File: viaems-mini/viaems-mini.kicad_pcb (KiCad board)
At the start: 2 copper layers, 214 parts, among them J1 Power Drivers, J10 TEST, J11 Sensors, J12 Debug, J13 USB_B_Micro, J14 Micro_SD_Card, J2 Primary, J3 Ignition Trace, J4 Injector Trace, J5 GPIO58, J6 SPI1, J7 PORTC, J8 PWM56, J9 CAN2, Q1 VNL5090S5-E, Q10 VNL5090S5-E, Q11 VNL5090S5-E, Q12 VNL5090S5-E, Q13 VNL5090S5-E, Q14 VNL5090S5-E, Q15 VNL5090S5-E, Q16 VNL5090S5-E, Q2 VNL5090S5-E, Q3 VNL5090S5-E, Q4 VNL5090S5-E, Q5 VNL5090S5-E, Q6 VNL5090S5-E, Q7 VNL5090S5-E, Q8 VNL5090S5-E, Q9 VNL5090S5-E, U1 TJA1051T-3, U10 MAX9926UAEE+, U11 LM2937-N, U2 LM2937-N, U3 NCV5501, U4 STM32F427VGTx, U5 MIC4469, U6 MIC4469, U7 MPXA6115A, U8 MPXA6400A, U9 AD7888, Y1 Crystal

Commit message: more
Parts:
- added J15: Micro SD, Connector_Card:microSD_HC_Hirose_DM3D-SF, B.Cu at (104.8, 85.1)
- C15, C56: footprint Capacitor_SMD:C_0805_2012Metric -> Capacitor_SMD:C_1206_3216Metric
- C39: value 0.22 uF -> 0.47 uF
- C40: value 0.47 uF -> 0.22 uF
- J1: value Power Drivers -> Primary; footprint Connector_PinHeader_2.54mm:PinHeader_2x10_P2.54mm_Vertical -> Connector_PinHeader_2.54mm:PinHeader_2x06_P2.54mm_Vertical
- J10: value TEST -> CAN2
- J11: value Sensors -> TEST; footprint Connector_PinHeader_2.54mm:PinHeader_2x08_P2.54mm_Vertical -> Connector_PinHeader_2.54mm:PinHeader_1x02_P2.54mm_Vertical
- J12: value Debug -> Sensors; footprint Connector_PinHeader_1.27mm:PinHeader_2x05_P1.27mm_Vertical_SMD -> Connector_PinHeader_2.54mm:PinHeader_2x08_P2.54mm_Vertical
- J13: value USB_B_Micro -> Debug; footprint Connector_USB:USB_Micro-B_Amphenol_10103594-0001LF_Horizontal -> Connector_PinHeader_1.27mm:PinHeader_2x05_P1.27mm_Vertical_SMD
- J14: value Micro_SD_Card -> USB_B; footprint Connector_Card:microSD_HC_Wuerth_693072010801 -> Connector_USB:USB_B_OST_USB-B1HSxx_Horizontal
- J2: value Primary -> Injectors; footprint Connector_PinHeader_2.54mm:PinHeader_2x06_P2.54mm_Vertical -> Connector_PinHeader_2.54mm:PinHeader_1x10_P2.54mm_Vertical
- J3: value Ignition Trace -> LSD; footprint Connector_PinHeader_2.54mm:PinHeader_1x09_P2.54mm_Vertical -> Connector_PinHeader_2.54mm:PinHeader_1x10_P2.54mm_Vertical
- J4: value Injector Trace -> Ignition Trace
- J5: value GPIO58 -> Injector Trace; footprint Connector_PinHeader_2.54mm:PinHeader_1x04_P2.54mm_Vertical -> Connector_PinHeader_2.54mm:PinHeader_1x09_P2.54mm_Vertical
- J6: value SPI1 -> GPIO58
- J7: value PORTC -> SPI1; footprint Connector_PinHeader_2.54mm:PinHeader_1x08_P2.54mm_Vertical -> Connector_PinHeader_2.54mm:PinHeader_1x04_P2.54mm_Vertical
- J8: value PWM56 -> PORTC; footprint Connector_PinHeader_2.54mm:PinHeader_1x02_P2.54mm_Vertical -> Connector_PinHeader_2.54mm:PinHeader_1x08_P2.54mm_Vertical
- J9: value CAN2 -> PWM56
- Q10, Q12, Q14, Q16, Q2, Q4, Q6, Q8, R15, R16, R19, R20, R23, R25, R40, R41, R44, R45, R49, R51, R68, R69, R70, R71, R72, R73, R74, R75, R76, R77, R78, R79, U1, U11, U3: moved to B.Cu
- R83: value 220 -> 470
- R84: value 470 -> 220
- U2: footprint Package_TO_SOT_THT:TO-220-3_Vertical -> Package_TO_SOT_THT:TO-220-3_Horizontal_TabDown
- moved J3 226.1 mm to (167.0, 162.6)
- moved Q11 188.6 mm to (158.8, 167.6)
- moved J1 182.3 mm to (165.0, 83.0)
- moved R77 181.3 mm to (149.9, 188.0)
- moved Q10 179.6 mm to (158.8, 158.8)
- moved R71 178.5 mm to (149.9, 170.2)
- moved R78 178.2 mm to (149.9, 185.4), turned to 180 degrees
- moved R79 177.9 mm to (149.9, 182.9), turned to 180 degrees
- moved J2 177.4 mm to (167.0, 126.2)
- moved Q16 176.5 mm to (158.8, 185.4)
- moved Q15 176.0 mm to (158.8, 185.4)
- moved Q9 175.3 mm to (158.5, 158.8)
- moved Q13 174.3 mm to (158.8, 176.5)
- moved J5 173.9 mm to (127.0, 149.0), turned to 180 degrees
- moved Q8 173.5 mm to (158.3, 150.5)
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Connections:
- J1 pad 1: /INJ-GND -> GND
- J1 pad 10: /INJ8 -> /IG5
- J1 pad 11: /LSD-GND -> /CANH
- J1 pad 12: /LSD-GND -> 12v_switched
- J1 pad 2: /INJ-GND -> /CANL
- J1 pad 3: /INJ1 -> /IG1
- J1 pad 4: /INJ2 -> /IG2
- J1 pad 5: /INJ3 -> /IG3
- J1 pad 6: /INJ4 -> /IG4
- J1 pad 7: /INJ5 -> /IG8
- J1 pad 8: /INJ6 -> /IG7
- J1 pad 9: /INJ7 -> /IG6
- J10 pad 1: /TEST1 -> /CAN2_RX
- J10 pad 2: /TEST2 -> /CAN2_TX
- J11 pad 1: GND -> /TEST1
- J11 pad 2: /5v_out -> /TEST2
- J12 pad 1: 3v_main -> GND
- J12 pad 10: /NRST -> /Inputs/BRV
- J12 pad 2: /SWDIO -> /5v_out
- J12 pad 4: /SWDCLK -> /5v_out
- J12 pad 5: GND -> /Inputs/IN1+
- J12 pad 6: /PWM5 -> /Inputs/TPS
- J12 pad 7: (no net) -> /Inputs/IN1-
- J12 pad 8: (no net) -> /Inputs/EGO
- J12 pad 9: GND -> /Inputs/IN2+
- J13 pad 1: Net-(J13-Pad1) -> 3v_main
- J13 pad 2: /USB_DM -> /SWDIO
- J13 pad 3: /USB_DP -> GND
- J13 pad 4: (no net) -> /SWDCLK
- J13 pad 6: GND -> /PWM5
- J14 pad 1: /SDIO_D2 -> Net-(J14-Pad1)
- J14 pad 2: /SDIO_D3 -> /USB_DM
- J14 pad 3: /SDIO_CMD -> /USB_DP
- J14 pad 4: 3v_main -> GND
- J14 pad 5: /SDIO_CK -> GND
- J2 pad 1: GND -> /INJ1
- J2 pad 10: /IG5 -> /INJ8
- J2 pad 2: /CANL -> /INJ2
- J2 pad 3: /IG1 -> /INJ3
- J2 pad 4: /IG2 -> /INJ4
- J2 pad 5: /IG3 -> /INJ-GND
- J2 pad 6: /IG4 -> /INJ-GND
- J2 pad 7: /IG8 -> /INJ5
- J2 pad 8: /IG7 -> /INJ6
- J2 pad 9: /IG6 -> /INJ7
- J3 pad 1: GND -> /LSD1
- J3 pad 2: /Outputs/IG8 -> /LSD2
- J3 pad 3: /Outputs/IG7 -> /LSD3
- J3 pad 4: /Outputs/IG6 -> /LSD4
- J3 pad 5: /Outputs/IG5 -> /LSD-GND
- J3 pad 6: /Outputs/IG4 -> /LSD-GND
- J3 pad 7: /Outputs/IG3 -> /LSD5
- J3 pad 8: /Outputs/IG2 -> /LSD6
- J3 pad 9: /Outputs/IG1 -> /LSD7
- J4 pad 2: /Outputs/INJ1 -> /Outputs/IG8
- J4 pad 3: /Outputs/INJ2 -> /Outputs/IG7
- J4 pad 4: /Outputs/INJ3 -> /Outputs/IG6
- J4 pad 5: /Outputs/INJ4 -> /Outputs/IG5
- J4 pad 6: /Outputs/INJ5 -> /Outputs/IG4
- J4 pad 7: /Outputs/INJ6 -> /Outputs/IG3
- J4 pad 8: /Outputs/INJ7 -> /Outputs/IG2
- J4 pad 9: /Outputs/INJ8 -> /Outputs/IG1
- J5 pad 1: Net-(J5-Pad1) -> GND
- J5 pad 2: Net-(J5-Pad2) -> /Outputs/INJ1
- J5 pad 3: Net-(J5-Pad3) -> /Outputs/INJ2
- J5 pad 4: Net-(J5-Pad4) -> /Outputs/INJ3
- J8 pad 1: /PWM5 -> Net-(J8-Pad1)
- J8 pad 2: /PWM6 -> Net-(J8-Pad2)
- J9 pad 1: /CAN2_RX -> /PWM5
- J9 pad 2: /CAN2_TX -> /PWM6
- Q1 pad 3: (no net) -> Net-(Q1-Pad3)
- Q1 pad 4: (no net) -> Net-(Q1-Pad4)
- Q10 pad 3: (no net) -> Net-(Q10-Pad3)
- Q10 pad 4: (no net) -> Net-(Q10-Pad4)
- Q10 pad 5: /LSD3 -> /LSD2
- Q10 pad 8: /LSD3 -> /LSD2
- Q11 pad 3: (no net) -> Net-(Q11-Pad3)
- Q11 pad 4: (no net) -> Net-(Q11-Pad4)
- Q11 pad 5: /LSD5 -> /LSD3
- Q11 pad 8: /LSD5 -> /LSD3
- Q12 pad 3: (no net) -> Net-(Q12-Pad3)
- Q12 pad 4: (no net) -> Net-(Q12-Pad4)
- Q12 pad 5: /LSD7 -> /LSD4
- Q12 pad 8: /LSD7 -> /LSD4
- Q13 pad 3: (no net) -> Net-(Q13-Pad3)
- Q13 pad 4: (no net) -> Net-(Q13-Pad4)
- Q13 pad 5: /LSD2 -> /LSD5
- Q13 pad 8: /LSD2 -> /LSD5
- Q14 pad 3: (no net) -> Net-(Q14-Pad3)
- Q14 pad 4: (no net) -> Net-(Q14-Pad4)
- Q14 pad 5: /LSD4 -> /LSD6
- Q14 pad 8: /LSD4 -> /LSD6
- Q15 pad 3: (no net) -> Net-(Q15-Pad3)
- Q15 pad 4: (no net) -> Net-(Q15-Pad4)
- Q15 pad 5: /LSD6 -> /LSD7
- Q15 pad 8: /LSD6 -> /LSD7
- Q16 pad 3: (no net) -> Net-(Q16-Pad3)
- Q16 pad 4: (no net) -> Net-(Q16-Pad4)
- Q2 pad 3: (no net) -> Net-(Q2-Pad3)
- Q2 pad 4: (no net) -> Net-(Q2-Pad4)
- Q3 pad 3: (no net) -> Net-(Q3-Pad3)
- Q3 pad 4: (no net) -> Net-(Q3-Pad4)
- Q3 pad 5: /INJ5 -> /INJ3
- Q3 pad 8: /INJ5 -> /INJ3
- Q4 pad 3: (no net) -> Net-(Q4-Pad3)
- Q4 pad 4: (no net) -> Net-(Q4-Pad4)
- Q4 pad 5: /INJ6 -> /INJ4
- Q4 pad 8: /INJ6 -> /INJ4
- Q5 pad 3: (no net) -> Net-(Q5-Pad3)
- Q5 pad 4: (no net) -> Net-(Q5-Pad4)
- Q5 pad 5: /INJ3 -> /INJ5
- Q5 pad 8: /INJ3 -> /INJ5
- Q6 pad 3: (no net) -> Net-(Q6-Pad3)
- Q6 pad 4: (no net) -> Net-(Q6-Pad4)
- Q6 pad 5: /INJ4 -> /INJ6
- Q6 pad 8: /INJ4 -> /INJ6
- Q7 pad 3: (no net) -> Net-(Q7-Pad3)
- Q7 pad 4: (no net) -> Net-(Q7-Pad4)
- Q8 pad 3: (no net) -> Net-(Q8-Pad3)
- Q8 pad 4: (no net) -> Net-(Q8-Pad4)
- Q9 pad 3: (no net) -> Net-(Q9-Pad3)
- Q9 pad 4: (no net) -> Net-(Q9-Pad4)
- R17 pad 1: Net-(Q3-Pad2) -> Net-(Q5-Pad2)
- R18 pad 1: Net-(Q3-Pad2) -> Net-(Q5-Pad2)
- R19 pad 1: Net-(Q4-Pad2) -> Net-(Q6-Pad2)
- R20 pad 1: Net-(Q4-Pad2) -> Net-(Q6-Pad2)
- R24 pad 2: Net-(Q3-Pad1) -> Net-(Q5-Pad1)
- R25 pad 2: Net-(Q4-Pad1) -> Net-(Q6-Pad1)
- R38 pad 1: Net-(Q5-Pad2) -> Net-(Q3-Pad2)
- R39 pad 1: Net-(Q5-Pad2) -> Net-(Q3-Pad2)
- R40 pad 1: Net-(Q6-Pad2) -> Net-(Q4-Pad2)
- R41 pad 1: Net-(Q6-Pad2) -> Net-(Q4-Pad2)
- R48 pad 2: Net-(Q5-Pad1) -> Net-(Q3-Pad1)
- R49 pad 2: Net-(Q6-Pad1) -> Net-(Q4-Pad1)
- R5 pad 2: Net-(J13-Pad1) -> Net-(J14-Pad1)
- R59 pad 2: Net-(Q10-Pad1) -> Net-(Q11-Pad1)
- R60 pad 1: Net-(Q10-Pad2) -> Net-(Q11-Pad2)
- R61 pad 1: Net-(Q10-Pad2) -> Net-(Q11-Pad2)
- R62 pad 2: Net-(Q11-Pad1) -> Net-(Q13-Pad1)
- R63 pad 1: Net-(Q11-Pad2) -> Net-(Q13-Pad2)
- R64 pad 1: Net-(Q11-Pad2) -> Net-(Q13-Pad2)
- R65 pad 2: Net-(Q12-Pad1) -> Net-(Q15-Pad1)
- R66 pad 1: Net-(Q12-Pad2) -> Net-(Q15-Pad2)
- R67 pad 1: Net-(Q12-Pad2) -> Net-(Q15-Pad2)
- R68 pad 2: Net-(Q13-Pad1) -> Net-(Q10-Pad1)
- R69 pad 1: Net-(Q13-Pad2) -> Net-(Q10-Pad2)
- R70 pad 1: Net-(Q13-Pad2) -> Net-(Q10-Pad2)
- R71 pad 2: Net-(Q14-Pad1) -> Net-(Q12-Pad1)
- R72 pad 1: Net-(Q14-Pad2) -> Net-(Q12-Pad2)
- R73 pad 1: Net-(Q14-Pad2) -> Net-(Q12-Pad2)
- R74 pad 2: Net-(Q15-Pad1) -> Net-(Q14-Pad1)
- R75 pad 1: Net-(Q15-Pad2) -> Net-(Q14-Pad2)
- R76 pad 1: Net-(Q15-Pad2) -> Net-(Q14-Pad2)
- U10 pad 12: (no net) -> Net-(U10-Pad12)
- U10 pad 2: (no net) -> Net-(U10-Pad2)
- U10 pad 7: (no net) -> Net-(U10-Pad7)
- U4 pad 15: Net-(J7-Pad1) -> Net-(J8-Pad1)
- U4 pad 16: Net-(J7-Pad2) -> Net-(J8-Pad2)
- U4 pad 17: Net-(J7-Pad3) -> Net-(J8-Pad3)
- U4 pad 18: Net-(J7-Pad4) -> Net-(J8-Pad4)
- U4 pad 29: Net-(J6-Pad1) -> Net-(J7-Pad1)
- U4 pad 30: Net-(J6-Pad2) -> Net-(J7-Pad2)
- U4 pad 31: Net-(J6-Pad3) -> Net-(J7-Pad3)
- U4 pad 32: Net-(J6-Pad4) -> Net-(J7-Pad4)
- U4 pad 33: Net-(J7-Pad5) -> Net-(J8-Pad5)
- U4 pad 34: Net-(J7-Pad6) -> Net-(J8-Pad6)
- U4 pad 59: Net-(J5-Pad4) -> Net-(J6-Pad4)
- U4 pad 60: Net-(J5-Pad3) -> Net-(J6-Pad3)
- U4 pad 61: Net-(J5-Pad2) -> Net-(J6-Pad2)
- U4 pad 62: Net-(J5-Pad1) -> Net-(J6-Pad1)
- U4 pad 63: Net-(J7-Pad7) -> Net-(J8-Pad7)
- U4 pad 64: Net-(J7-Pad8) -> Net-(J8-Pad8)
- U4 pad 7: (no net) -> Net-(U4-Pad7)
- U4 pad 77: (no net) -> Net-(U4-Pad77)
- U4 pad 8: (no net) -> Net-(U4-Pad8)
- U4 pad 81: (no net) -> Net-(U4-Pad81)
- U4 pad 82: (no net) -> Net-(U4-Pad82)
- U4 pad 84: (no net) -> Net-(U4-Pad84)
- U4 pad 85: (no net) -> Net-(U4-Pad85)
- U4 pad 86: (no net) -> Net-(U4-Pad86)
- U4 pad 87: (no net) -> Net-(U4-Pad87)
- U4 pad 88: (no net) -> Net-(U4-Pad88)
- U4 pad 9: (no net) -> Net-(U4-Pad9)
- U4 pad 93: (no net) -> Net-(U4-Pad93)
- U7 pad 1: (no net) -> Net-(U7-Pad1)
- U7 pad 5: (no net) -> Net-(U7-Pad5)
- U7 pad 6: (no net) -> Net-(U7-Pad6)
- U7 pad 7: (no net) -> Net-(U7-Pad7)
- U7 pad 8: (no net) -> Net-(U7-Pad8)
- U8 pad 1: (no net) -> Net-(U8-Pad1)
- U8 pad 5: (no net) -> Net-(U8-Pad5)
- U8 pad 6: (no net) -> Net-(U8-Pad6)
- U8 pad 7: (no net) -> Net-(U8-Pad7)
- U8 pad 8: (no net) -> Net-(U8-Pad8)
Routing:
- net /LSD-GND: track 0.00 -> 48.7 mm, vias 0 -> 32
- net /INJ-GND: track 0.00 -> 24.7 mm, vias 0 -> 32
- net /LSD2: track 0.00 -> 17.1 mm
- net /INJ2: track 0.00 -> 16.4 mm
- net /LSD1: track 0.00 -> 14.2 mm
- net /INJ7: track 0.00 -> 13.9 mm
- net /LSD6: track 0.00 -> 13.6 mm
- net /INJ1: track 0.00 -> 12.6 mm
- net /INJ6: track 0.00 -> 12.6 mm
- net /LSD4: track 0.00 -> 11.8 mm
- net /LSD7: track 0.00 -> 11.8 mm
- net /INJ8: track 0.00 -> 11.6 mm
- net /INJ4: track 0.00 -> 11.6 mm
- net /LSD8: track 0.00 -> 10.7 mm
- net /LSD5: track 0.00 -> 10.7 mm
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- added copper zone on B.Cu, net /INJ-GND
- added copper zone on F.Cu, net /INJ-GND
- added copper zone on In1.Cu, net /INJ-GND
- added copper zone on B.Cu, net /LSD-GND
- added copper zone on F.Cu, net /LSD-GND
- added copper zone on In1.Cu, net /LSD-GND
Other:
- board outline added: 73 x 154 mm
- copper layers 2 -> 4

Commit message: more
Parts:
- C31, C32, C33, C41, C42, C43, R32, R33, R34, R35, R36, R37, R46, R47, R52, R53, R54, R55, U6: moved to B.Cu
- D1: footprint Diode_SMD:D_0805_2012Metric -> Diode_THT:D_DO-41_SOD81_P2.54mm_Vertical_AnodeUp
- R102, R103: footprint Resistor_SMD:R_0805_2012Metric -> Resistor_THT:R_Axial_DIN0204_L3.6mm_D1.6mm_P2.54mm_Vertical
- U11: moved to F.Cu
- moved R67 163.1 mm to (151.0, 188.0), turned to 180 degrees
- moved R66 161.0 mm to (151.0, 185.5), turned to 180 degrees
- moved R65 158.5 mm to (151.0, 183.0)
- moved R48 156.8 mm to (151.0, 130.0)
- moved R63 155.6 mm to (151.0, 176.5), turned to 180 degrees
- moved R64 155.4 mm to (151.0, 179.0), turned to 180 degrees
- moved R62 153.4 mm to (151.0, 174.0)
- moved R61 148.0 mm to (151.0, 170.0), turned to 180 degrees
- moved R60 145.6 mm to (151.0, 167.5), turned to 180 degrees
- moved R59 145.4 mm to (151.0, 165.0)
- moved R42 140.3 mm to (151.0, 150.5), turned to 180 degrees
- moved D1 140.1 mm to (154.0, 41.5), turned to 180 degrees
- moved R43 139.9 mm to (151.0, 153.0), turned to 180 degrees
- moved R17 138.9 mm to (151.0, 141.5), turned to 180 degrees
- moved R18 137.6 mm to (151.0, 144.0), turned to 180 degrees
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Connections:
- C31 pad 1: /Inputs/TPS -> /TPS
- C32 pad 1: /Inputs/EGO -> /EGO
- C33 pad 1: /Inputs/SPR -> /SPR
- C42 pad 1: /Inputs/CLT -> /CLT
- C43 pad 1: /Inputs/IAT -> /IAT
- J1 pad 10: /IG5 -> /IG8
- J1 pad 11: /CANH -> /CANL
- J1 pad 12: 12v_switched -> /CANH
- J1 pad 2: /CANL -> 12v_switched
- J1 pad 4: /IG2 -> /IG5
- J1 pad 5: /IG3 -> /IG2
- J1 pad 6: /IG4 -> /IG6
- J1 pad 7: /IG8 -> /IG3
- J1 pad 9: /IG6 -> /IG4
- J12 pad 10: /Inputs/BRV -> /SPR
- J12 pad 11: /Inputs/IN2- -> /IN1-
- J12 pad 12: /Inputs/CLT -> /IN1+
- J12 pad 13: /Inputs/DIG1 -> /IN2-
- J12 pad 14: /Inputs/IAT -> /IN2+
- J12 pad 15: /Inputs/DIG2 -> /DIG1
- J12 pad 16: /Inputs/SPR -> /DIG2
- J12 pad 5: /Inputs/IN1+ -> /TPS
- J12 pad 6: /Inputs/TPS -> /EGO
- J12 pad 7: /Inputs/IN1- -> /BRV
- J12 pad 8: /Inputs/EGO -> /CLT
- J12 pad 9: /Inputs/IN2+ -> /IAT
- R100 pad 1: /Inputs/IN2- -> /IN2-
- R101 pad 1: /Inputs/IN2+ -> /IN2+
- R102 pad 1: /Inputs/IN1- -> /IN1-
- R102 pad 2: /Inputs/IN1+ -> /IN1+
- R103 pad 1: /Inputs/IN2- -> /IN2-
- R103 pad 2: /Inputs/IN2+ -> /IN2+
- R80 pad 2: /Inputs/TPS -> /TPS
- R81 pad 2: /Inputs/EGO -> /EGO
- R82 pad 2: /Inputs/SPR -> /SPR
- R85 pad 1: /Inputs/BRV -> /BRV
- R87 pad 2: /Inputs/CLT -> /CLT
- R88 pad 2: /Inputs/IAT -> /IAT
- R90 pad 2: /Inputs/CLT -> /CLT
- R91 pad 2: /Inputs/IAT -> /IAT
- R96 pad 2: /Inputs/DIG1 -> /DIG1
- R97 pad 2: /Inputs/DIG2 -> /DIG2
- R98 pad 1: /Inputs/IN1+ -> /IN1+
- R99 pad 1: /Inputs/IN1- -> /IN1-
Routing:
- net 12v_switched: track 0.00 -> 71.9 mm
- net 5v_main: track 0.00 -> 39.3 mm, vias 0 -> 1
- net GND: track 0.00 -> 33.1 mm, vias 0 -> 7
- net Net-(C25-Pad1): track 0.00 -> 30.4 mm, vias 0 -> 1
- net /IN1+: track 0.00 -> 27.4 mm
- net /IN1-: track 0.00 -> 23.2 mm
- net Net-(C52-Pad1): track 0.00 -> 22.0 mm
- net Net-(C52-Pad2): track 0.00 -> 21.9 mm
- net Net-(R46-Pad1): track 0.00 -> 18.1 mm
- net Net-(R26-Pad1): track 0.00 -> 18.1 mm
- net /IN2+: track 0.00 -> 16.3 mm
- net /IN2-: track 0.00 -> 12.3 mm
- net Net-(C51-Pad1): track 0.00 -> 11.9 mm
- net Net-(R52-Pad2): track 0.00 -> 11.2 mm
- net /EGO: track 0.00 -> 10.8 mm
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
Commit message: more
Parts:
- C29, C30, C37, C38, C39, C40, R83, R84, R86, U11: moved to B.Cu
- moved D9 96.6 mm to (158.5, 71.5), turned to 90 degrees
- moved D8 96.5 mm to (162.5, 71.5), turned to 90 degrees
- moved R80 78.4 mm to (159.5, 51.0)
- moved R81 74.1 mm to (159.5, 54.0)
- moved D6 72.7 mm to (135.0, 58.5)
- moved R85 70.8 mm to (158.0, 57.5), turned to 180 degrees
- moved R82 70.6 mm to (153.0, 62.5)
- moved D7 69.3 mm to (140.0, 60.5)
- moved R91 67.5 mm to (153.0, 59.5)
- moved C46 66.9 mm to (146.5, 59.0), turned to 180 degrees
- moved C45 66.2 mm to (146.5, 56.0), turned to 180 degrees
- moved D4 65.6 mm to (135.0, 62.5)
- moved R89 65.4 mm to (153.0, 53.5)
- moved R90 65.0 mm to (153.0, 56.5)
- moved R86 62.9 mm to (155.0, 53.0), turned to 180 degrees
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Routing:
- net /Inputs/EGO-adc: track 0.00 -> 48.7 mm, vias 0 -> 2
- net /Inputs/TPS-adc: track 0.00 -> 42.4 mm, vias 0 -> 2
- net /Inputs/CLT-adc: track 0.00 -> 34.4 mm, vias 0 -> 2
- net /Inputs/BRV-adc: track 0.00 -> 34.2 mm
- net /Inputs/IAT-adc: track 0.00 -> 32.2 mm
- net /Inputs/SPR-adc: track 0.00 -> 25.5 mm
- net /Inputs/MAP-adc: track 0.00 -> 18.4 mm, vias 0 -> 1
- net GND: track 33.1 -> 51.1 mm, vias 7 -> 11
- net /Inputs/AAP-adc: track 0.00 -> 16.8 mm, vias 0 -> 1
- net /CLT: track 8.45 -> 23.5 mm
- net /SPR: track 7.44 -> 22.0 mm
- net Net-(C41-Pad1): track 0.00 -> 13.0 mm, vias 0 -> 1
- net 12v_switched: track 71.9 -> 84.0 mm
- net /IAT: track 4.96 -> 16.3 mm
- net /EGO: track 10.8 -> 19.3 mm
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
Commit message: more
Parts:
- C13, C15, C22, C24, C4, C47, C48, C49, C50, C54, C56, C7: moved to B.Cu
- U1: moved to F.Cu
- moved C4 163.1 mm to (162.0, 92.0), turned to 90 degrees
- moved C7 153.9 mm to (159.0, 92.0), turned to 90 degrees
- moved R1 140.3 mm to (159.0, 115.0), turned to 90 degrees
- moved C24 139.5 mm to (105.5, 148.0)
- moved C13 137.1 mm to (162.0, 88.0), turned to 270 degrees
- moved R7 136.0 mm to (109.5, 145.5), turned to 180 degrees
- moved C22 131.4 mm to (105.5, 137.5)
- moved C15 126.3 mm to (159.0, 87.5), turned to 270 degrees
- moved R2 124.9 mm to (119.0, 131.5), turned to 180 degrees
- moved R3 121.5 mm to (119.0, 128.5), turned to 180 degrees
- moved C56 98.6 mm to (167.0, 80.0), turned to 90 degrees
- moved C50 91.3 mm to (167.0, 75.5), turned to 270 degrees
- moved C49 89.9 mm to (164.5, 75.5), turned to 270 degrees
- moved R97 88.9 mm to (166.0, 71.5)
- moved C54 84.4 mm to (164.5, 79.5), turned to 90 degrees
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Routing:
- net GND: track 51.1 -> 175.8 mm, vias 11 -> 44
- net /Outputs/IG1: track 0.00 -> 86.2 mm, vias 0 -> 1
- net 5v_main: track 39.3 -> 119.1 mm, vias 1 -> 2
- net /Outputs/IG2: track 0.00 -> 78.0 mm, vias 0 -> 1
- net /Outputs/IG8: track 0.00 -> 76.6 mm, vias 0 -> 1
- net /Outputs/IG3: track 0.00 -> 74.2 mm, vias 0 -> 1
- net /Outputs/IG4: track 0.00 -> 67.2 mm, vias 0 -> 1
- net /Outputs/IG7: track 0.00 -> 60.0 mm, vias 0 -> 1
- net /USB_DP: track 0.00 -> 60.0 mm
- net /Outputs/IG6: track 0.00 -> 59.4 mm, vias 0 -> 1
- net /USB_DM: track 0.00 -> 59.4 mm
- net /Outputs/IG5: track 0.00 -> 57.9 mm, vias 0 -> 1
- net Net-(J8-Pad8): track 0.00 -> 50.7 mm, vias 0 -> 1
- net /PWM3: track 0.00 -> 49.0 mm
- net /PWM1: track 0.00 -> 48.0 mm, vias 0 -> 2
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- added copper zone on In2.Cu, net 3v_main
- added copper zone on In2.Cu, net 5v_adc
- added copper zone on In2.Cu, net 5v_main
- added copper zone on In1.Cu, net GND

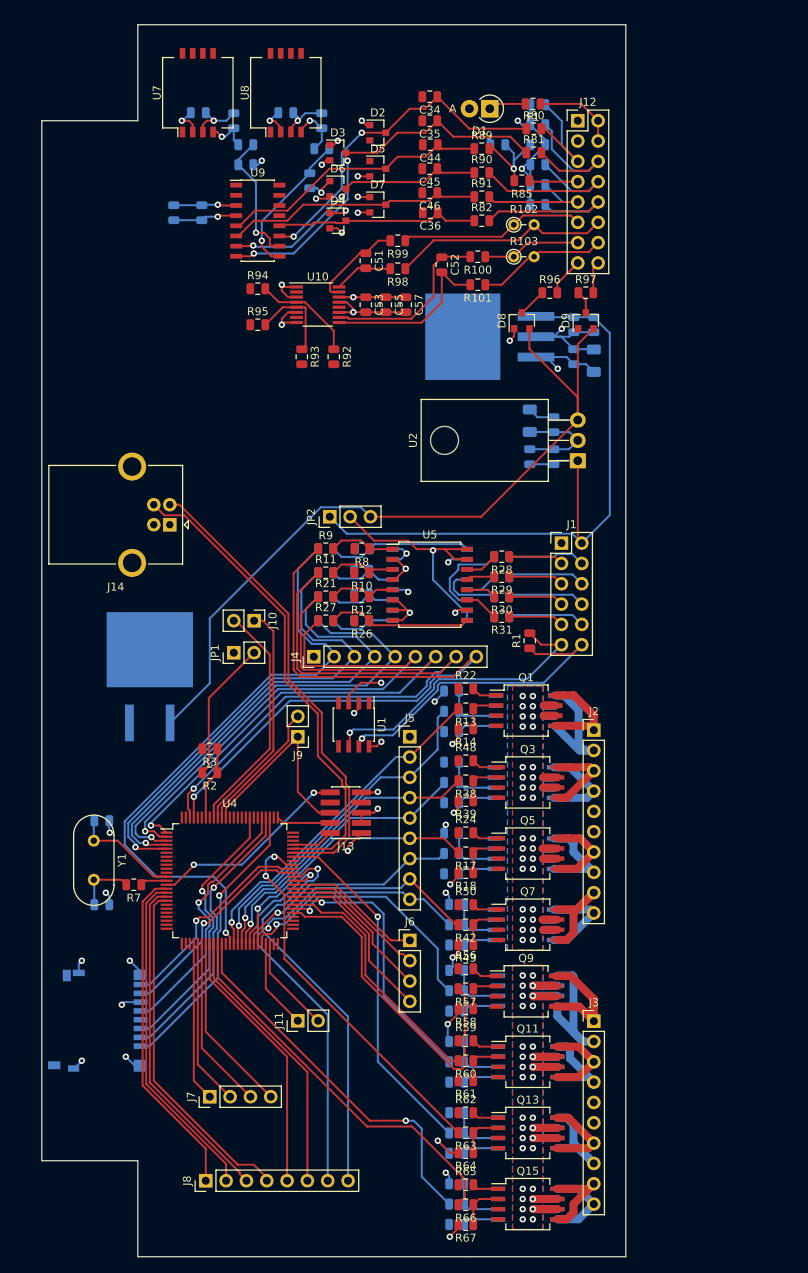
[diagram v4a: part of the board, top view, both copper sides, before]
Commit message: move analog to opposite end
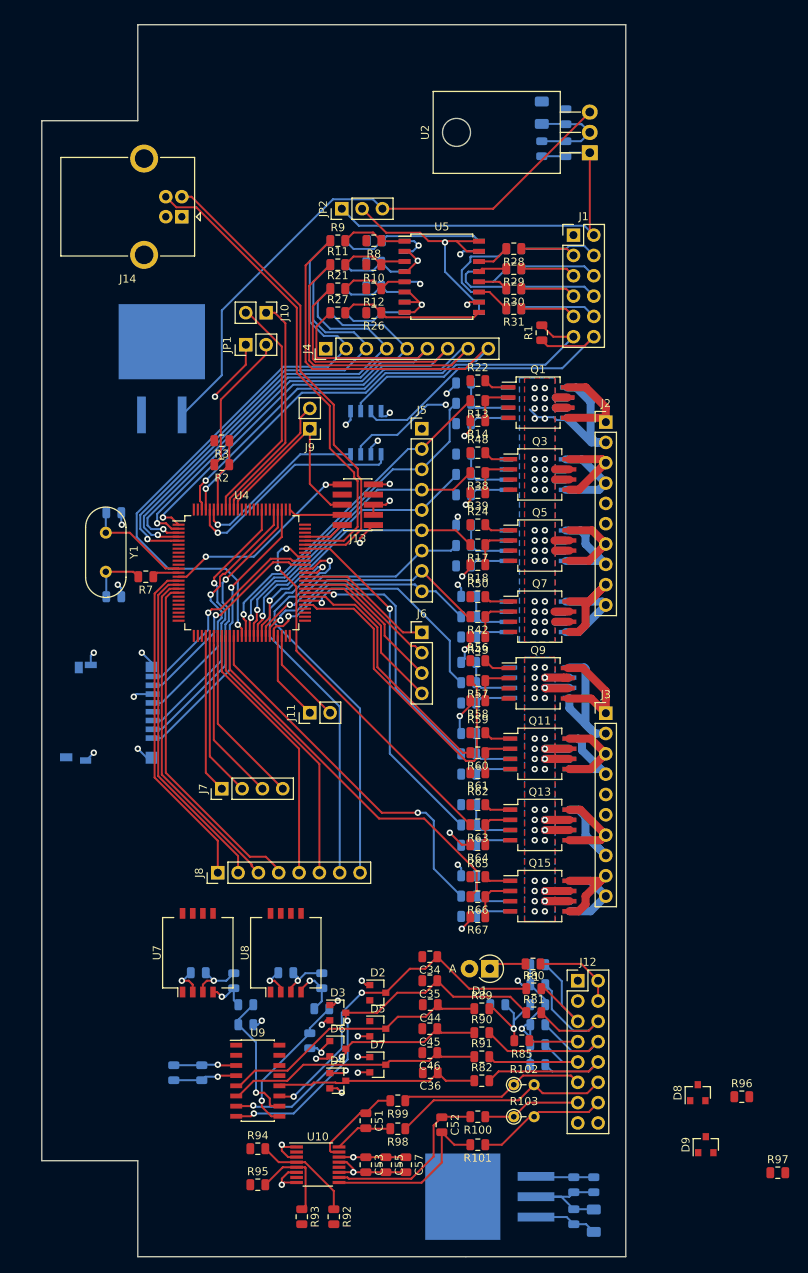
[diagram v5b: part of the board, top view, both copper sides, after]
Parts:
- U1: moved to B.Cu
- moved R97 112.6 mm to (190.0, 181.5)
- moved C29 107.5 mm to (128.5, 156.5)
- moved C30 107.5 mm to (117.6, 156.5)
- moved C31 107.5 mm to (160.0, 155.5)
- moved C32 107.5 mm to (160.0, 158.0)
- moved C33 107.5 mm to (160.0, 168.0)
- moved C34 107.5 mm to (146.5, 154.5)
- moved C35 107.5 mm to (146.5, 157.5)
- moved C36 107.5 mm to (146.6, 169.0)
- moved C37 107.5 mm to (122.0, 157.5)
- moved C38 107.5 mm to (133.0, 157.5)
- moved C39 107.5 mm to (123.5, 163.0)
- moved C40 107.5 mm to (131.5, 165.0)
- moved C41 107.5 mm to (160.0, 160.5)
- moved C42 107.5 mm to (160.0, 163.0)
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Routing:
- net 12v_switched: track 87.3 -> 56.8 mm
- net /CAN_TX: track 0.00 -> 28.4 mm, vias 0 -> 1
- net 5v_main: track 119.1 -> 94.5 mm
- net /CAN_RX: track 0.00 -> 22.3 mm, vias 0 -> 1
- net 3v_main: track 2.92 -> 13.0 mm, vias 1 -> 3
- net /INJ-GND: track 24.7 -> 31.2 mm
- net /DIG1: track 4.78 -> 0.00 mm
- net GND: track 175.8 -> 171.2 mm, vias 44 -> 42
- net /DIG2: track 3.97 -> 0.00 mm
- net /Inputs/DIG1-cpu: track 3.60 -> 0.00 mm
- net 5v_adc: track 39.5 -> 36.2 mm, vias 9 -> 8
- net /Inputs/DIG2-cpu: track 2.89 -> 0.00 mm
- net /CANL: track 37.7 -> 35.6 mm, vias 1 -> 0
- net /CANH: track 41.1 -> 40.1 mm, vias 1 -> 0
- removed copper zone on In1.Cu, net /INJ-GND
- removed copper zone on In1.Cu, net /LSD-GND
- removed copper zone on In2.Cu, net 3v_main
- removed copper zone on In2.Cu, net 5v_adc
- removed copper zone on In2.Cu, net 5v_main
- removed copper zone on In1.Cu, net GND
